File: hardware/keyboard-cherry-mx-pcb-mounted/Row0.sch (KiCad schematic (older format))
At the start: 28 parts, among them SW10 F4, SW11 F12, SW12 F5, SW13 Delete, SW14 F6, SW15 F7, SW2 ESC, SW3 F8, SW4 F1, SW5 F9, SW6 F2, SW7 F10, SW8 F3, SW9 F11

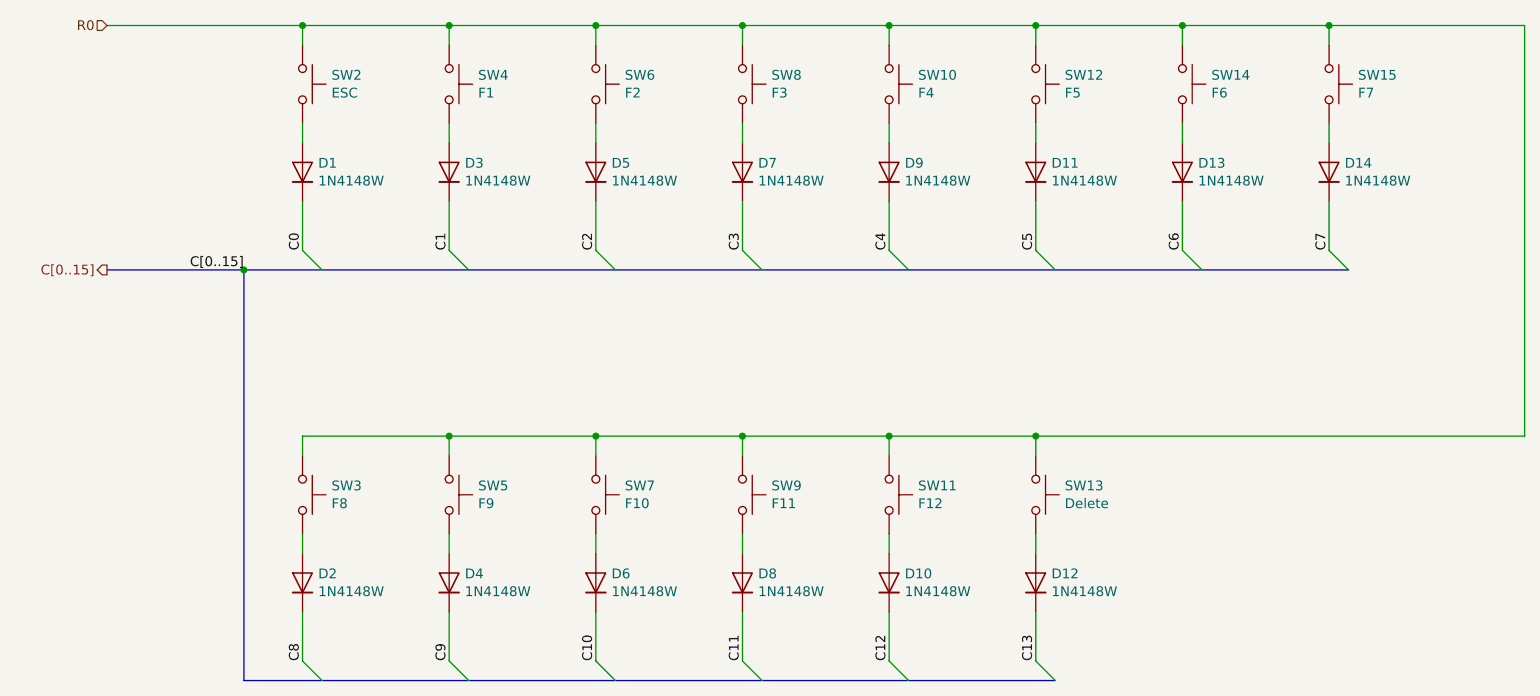
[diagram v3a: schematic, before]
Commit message: Aligns the keys so the column connections are more consistent. e.g. right most keys will have same column connection.
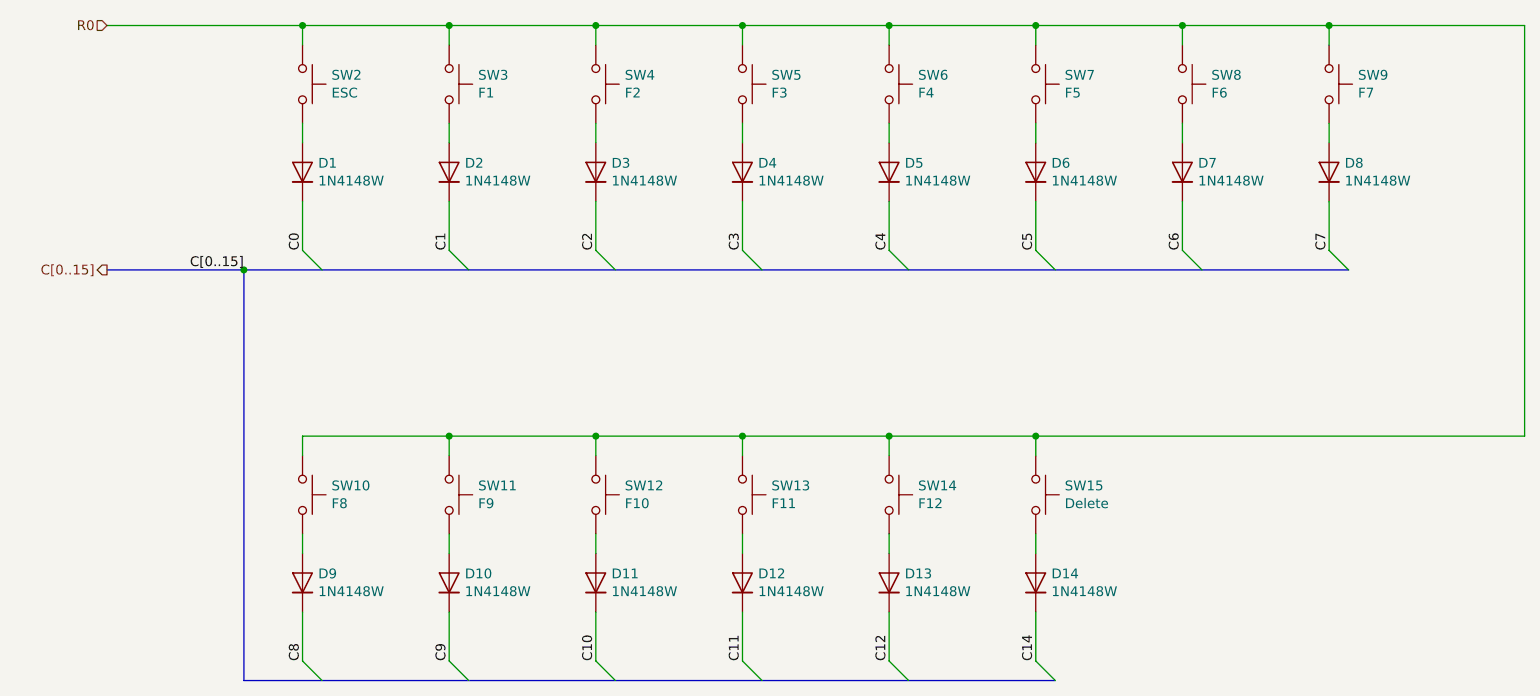
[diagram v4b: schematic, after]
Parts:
- renumbered D4 to D10, D6 to D11, D8 to D12, D10 to D13, D12 to D14, D3 to D2, D5 to D3, D7 to D4, D9 to D5, D11 to D6, D13 to D7, D14 to D8, D2 to D9, SW3 to SW10, SW5 to SW11, SW7 to SW12, SW9 to SW13, SW11 to SW14, SW13 to SW15, SW4 to SW3, SW6 to SW4, SW8 to SW5, SW10 to SW6, SW12 to SW7, SW14 to SW8, SW15 to SW9
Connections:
- net C13 renamed C14
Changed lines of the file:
@@
 P 3850 2700
 AR Path="/5E697948/5E6D9959" Ref="SW?"  Part="1"
-AR Path="/5E697948/5E6CDE4B/5E6D9959" Ref="SW4"  Part="1"
-F 0 "SW4" V 3804 2848 50  0000 L CNN
+AR Path="/5E697948/5E6CDE4B/5E6D9959" Ref="SW3"  Part="1"
+F 0 "SW3" V 3804 2848 50  0000 L CNN
 F 1 "F1" V 3895 2848 50  0000 L CNN
 F 2 "Button_Switch_Keyboard:SW_Cherry_MX_1.00u_PCB" H 3850 2900 50  0001 C CNN
@@
 P 3850 3150
 AR Path="/5E697948/5E6D995F" Ref="D?"  Part="1"
-AR Path="/5E697948/5E6CDE4B/5E6D995F" Ref="D3"  Part="1"
-F 0 "D3" V 3896 3070 50  0000 R CNN
+AR Path="/5E697948/5E6CDE4B/5E6D995F" Ref="D2"  Part="1"
+F 0 "D2" V 3896 3070 50  0000 R CNN
 F 1 "1N4148W" V 3805 3070 50  0000 R CNN
 F 2 "Diode_SMD:D_SOD-123" H 3850 2975 50  0001 C CNN
@@
 P 4600 2700
 AR Path="/5E697948/5E6D9967" Ref="SW?"  Part="1"
-AR Path="/5E697948/5E6CDE4B/5E6D9967" Ref="SW6"  Part="1"
-F 0 "SW6" V 4554 2848 50  0000 L CNN
+AR Path="/5E697948/5E6CDE4B/5E6D9967" Ref="SW4"  Part="1"
+F 0 "SW4" V 4554 2848 50  0000 L CNN
 F 1 "F2" V 4645 2848 50  0000 L CNN
 F 2 "Button_Switch_Keyboard:SW_Cherry_MX_1.00u_PCB" H 4600 2900 50  0001 C CNN
@@
 P 4600 3150
 AR Path="/5E697948/5E6D996D" Ref="D?"  Part="1"
-AR Path="/5E697948/5E6CDE4B/5E6D996D" Ref="D5"  Part="1"
-F 0 "D5" V 4646 3070 50  0000 R CNN
+AR Path="/5E697948/5E6CDE4B/5E6D996D" Ref="D3"  Part="1"
+F 0 "D3" V 4646 3070 50  0000 R CNN
 F 1 "1N4148W" V 4555 3070 50  0000 R CNN
 F 2 "Diode_SMD:D_SOD-123" H 4600 2975 50  0001 C CNN
@@
 P 5350 2700
 AR Path="/5E697948/5E6D9975" Ref="SW?"  Part="1"
-AR Path="/5E697948/5E6CDE4B/5E6D9975" Ref="SW8"  Part="1"
-F 0 "SW8" V 5304 2848 50  0000 L CNN
+AR Path="/5E697948/5E6CDE4B/5E6D9975" Ref="SW5"  Part="1"
+F 0 "SW5" V 5304 2848 50  0000 L CNN
 F 1 "F3" V 5395 2848 50  0000 L CNN
 F 2 "Button_Switch_Keyboard:SW_Cherry_MX_1.00u_PCB" H 5350 2900 50  0001 C CNN
@@
 P 5350 3150
 AR Path="/5E697948/5E6D997B" Ref="D?"  Part="1"
-AR Path="/5E697948/5E6CDE4B/5E6D997B" Ref="D7"  Part="1"
-F 0 "D7" V 5396 3070 50  0000 R CNN
+AR Path="/5E697948/5E6CDE4B/5E6D997B" Ref="D4"  Part="1"
+F 0 "D4" V 5396 3070 50  0000 R CNN
 F 1 "1N4148W" V 5305 3070 50  0000 R CNN
 F 2 "Diode_SMD:D_SOD-123" H 5350 2975 50  0001 C CNN
@@
 P 6100 2700
 AR Path="/5E697948/5E6D9983" Ref="SW?"  Part="1"
-AR Path="/5E697948/5E6CDE4B/5E6D9983" Ref="SW10"  Part="1"
-F 0 "SW10" V 6054 2848 50  0000 L CNN
+AR Path="/5E697948/5E6CDE4B/5E6D9983" Ref="SW6"  Part="1"
+F 0 "SW6" V 6054 2848 50  0000 L CNN
 F 1 "F4" V 6145 2848 50  0000 L CNN
 F 2 "Button_Switch_Keyboard:SW_Cherry_MX_1.00u_PCB" H 6100 2900 50  0001 C CNN
@@
 P 6100 3150
 AR Path="/5E697948/5E6D9989" Ref="D?"  Part="1"
-AR Path="/5E697948/5E6CDE4B/5E6D9989" Ref="D9"  Part="1"
-F 0 "D9" V 6146 3070 50  0000 R CNN
+AR Path="/5E697948/5E6CDE4B/5E6D9989" Ref="D5"  Part="1"
+F 0 "D5" V 6146 3070 50  0000 R CNN
 F 1 "1N4148W" V 6055 3070 50  0000 R CNN
 F 2 "Diode_SMD:D_SOD-123" H 6100 2975 50  0001 C CNN
@@
 P 6850 2700
 AR Path="/5E697948/5E6D9991" Ref="SW?"  Part="1"
-AR Path="/5E697948/5E6CDE4B/5E6D9991" Ref="SW12"  Part="1"
-F 0 "SW12" V 6804 2848 50  0000 L CNN
+AR Path="/5E697948/5E6CDE4B/5E6D9991" Ref="SW7"  Part="1"
+F 0 "SW7" V 6804 2848 50  0000 L CNN
 F 1 "F5" V 6895 2848 50  0000 L CNN
 F 2 "Button_Switch_Keyboard:SW_Cherry_MX_1.00u_PCB" H 6850 2900 50  0001 C CNN
@@
 P 6850 3150
 AR Path="/5E697948/5E6D9997" Ref="D?"  Part="1"
-AR Path="/5E697948/5E6CDE4B/5E6D9997" Ref="D11"  Part="1"
-F 0 "D11" V 6896 3070 50  0000 R CNN
+AR Path="/5E697948/5E6CDE4B/5E6D9997" Ref="D6"  Part="1"
+F 0 "D6" V 6896 3070 50  0000 R CNN
 F 1 "1N4148W" V 6805 3070 50  0000 R CNN
 F 2 "Diode_SMD:D_SOD-123" H 6850 2975 50  0001 C CNN
@@
 P 7600 2700
 AR Path="/5E697948/5E6D999F" Ref="SW?"  Part="1"
-AR Path="/5E697948/5E6CDE4B/5E6D999F" Ref="SW14"  Part="1"
-F 0 "SW14" V 7554 2848 50  0000 L CNN
+AR Path="/5E697948/5E6CDE4B/5E6D999F" Ref="SW8"  Part="1"
+F 0 "SW8" V 7554 2848 50  0000 L CNN
 F 1 "F6" V 7645 2848 50  0000 L CNN
 F 2 "Button_Switch_Keyboard:SW_Cherry_MX_1.00u_PCB" H 7600 2900 50  0001 C CNN
@@
 P 7600 3150
 AR Path="/5E697948/5E6D99A5" Ref="D?"  Part="1"
-AR Path="/5E697948/5E6CDE4B/5E6D99A5" Ref="D13"  Part="1"
-F 0 "D13" V 7646 3070 50  0000 R CNN
+AR Path="/5E697948/5E6CDE4B/5E6D99A5" Ref="D7"  Part="1"
+F 0 "D7" V 7646 3070 50  0000 R CNN
 F 1 "1N4148W" V 7555 3070 50  0000 R CNN
 F 2 "Diode_SMD:D_SOD-123" H 7600 2975 50  0001 C CNN
@@
 P 8350 2700
 AR Path="/5E697948/5E6D99AD" Ref="SW?"  Part="1"
-AR Path="/5E697948/5E6CDE4B/5E6D99AD" Ref="SW15"  Part="1"
-F 0 "SW15" V 8304 2848 50  0000 L CNN
+AR Path="/5E697948/5E6CDE4B/5E6D99AD" Ref="SW9"  Part="1"
+F 0 "SW9" V 8304 2848 50  0000 L CNN
 F 1 "F7" V 8395 2848 50  0000 L CNN
 F 2 "Button_Switch_Keyboard:SW_Cherry_MX_1.00u_PCB" H 8350 2900 50  0001 C CNN
@@
 P 8350 3150
 AR Path="/5E697948/5E6D99B3" Ref="D?"  Part="1"
-AR Path="/5E697948/5E6CDE4B/5E6D99B3" Ref="D14"  Part="1"
-F 0 "D14" V 8396 3070 50  0000 R CNN
+AR Path="/5E697948/5E6CDE4B/5E6D99B3" Ref="D8"  Part="1"
+F 0 "D8" V 8396 3070 50  0000 R CNN
 F 1 "1N4148W" V 8305 3070 50  0000 R CNN
 F 2 "Diode_SMD:D_SOD-123" H 8350 2975 50  0001 C CNN
@@
 P 3100 4800
 AR Path="/5E697948/5E6D99BB" Ref="SW?"  Part="1"
-AR Path="/5E697948/5E6CDE4B/5E6D99BB" Ref="SW3"  Part="1"
-F 0 "SW3" V 3054 4948 50  0000 L CNN
+AR Path="/5E697948/5E6CDE4B/5E6D99BB" Ref="SW10"  Part="1"
+F 0 "SW10" V 3054 4948 50  0000 L CNN
 F 1 "F8" V 3145 4948 50  0000 L CNN
 F 2 "Button_Switch_Keyboard:SW_Cherry_MX_1.00u_PCB" H 3100 5000 50  0001 C CNN
@@
 P 3100 5250
 AR Path="/5E697948/5E6D99C1" Ref="D?"  Part="1"
-AR Path="/5E697948/5E6CDE4B/5E6D99C1" Ref="D2"  Part="1"
-F 0 "D2" V 3146 5170 50  0000 R CNN
+AR Path="/5E697948/5E6CDE4B/5E6D99C1" Ref="D9"  Part="1"
+F 0 "D9" V 3146 5170 50  0000 R CNN
 F 1 "1N4148W" V 3055 5170 50  0000 R CNN
 F 2 "Diode_SMD:D_SOD-123" H 3100 5075 50  0001 C CNN
@@
 P 3850 4800
 AR Path="/5E697948/5E6D99C9" Ref="SW?"  Part="1"
-AR Path="/5E697948/5E6CDE4B/5E6D99C9" Ref="SW5"  Part="1"
-F 0 "SW5" V 3804 4948 50  0000 L CNN
+AR Path="/5E697948/5E6CDE4B/5E6D99C9" Ref="SW11"  Part="1"
+F 0 "SW11" V 3804 4948 50  0000 L CNN
 F 1 "F9" V 3895 4948 50  0000 L CNN
 F 2 "Button_Switch_Keyboard:SW_Cherry_MX_1.00u_PCB" H 3850 5000 50  0001 C CNN
@@
 P 3850 5250
 AR Path="/5E697948/5E6D99CF" Ref="D?"  Part="1"
-AR Path="/5E697948/5E6CDE4B/5E6D99CF" Ref="D4"  Part="1"
-F 0 "D4" V 3896 5170 50  0000 R CNN
+AR Path="/5E697948/5E6CDE4B/5E6D99CF" Ref="D10"  Part="1"
+F 0 "D10" V 3896 5170 50  0000 R CNN
 F 1 "1N4148W" V 3805 5170 50  0000 R CNN
 F 2 "Diode_SMD:D_SOD-123" H 3850 5075 50  0001 C CNN
@@
 P 4600 4800
 AR Path="/5E697948/5E6D99D7" Ref="SW?"  Part="1"
-AR Path="/5E697948/5E6CDE4B/5E6D99D7" Ref="SW7"  Part="1"
-F 0 "SW7" V 4554 4948 50  0000 L CNN
+AR Path="/5E697948/5E6CDE4B/5E6D99D7" Ref="SW12"  Part="1"
+F 0 "SW12" V 4554 4948 50  0000 L CNN
 F 1 "F10" V 4645 4948 50  0000 L CNN
 F 2 "Button_Switch_Keyboard:SW_Cherry_MX_1.00u_PCB" H 4600 5000 50  0001 C CNN
@@
 P 4600 5250
 AR Path="/5E697948/5E6D99DD" Ref="D?"  Part="1"
-AR Path="/5E697948/5E6CDE4B/5E6D99DD" Ref="D6"  Part="1"
-F 0 "D6" V 4646 5170 50  0000 R CNN
+AR Path="/5E697948/5E6CDE4B/5E6D99DD" Ref="D11"  Part="1"
+F 0 "D11" V 4646 5170 50  0000 R CNN
 F 1 "1N4148W" V 4555 5170 50  0000 R CNN
 F 2 "Diode_SMD:D_SOD-123" H 4600 5075 50  0001 C CNN
@@
 P 5350 4800
 AR Path="/5E697948/5E6D99E5" Ref="SW?"  Part="1"
-AR Path="/5E697948/5E6CDE4B/5E6D99E5" Ref="SW9"  Part="1"
-F 0 "SW9" V 5304 4948 50  0000 L CNN
+AR Path="/5E697948/5E6CDE4B/5E6D99E5" Ref="SW13"  Part="1"
+F 0 "SW13" V 5304 4948 50  0000 L CNN
 F 1 "F11" V 5395 4948 50  0000 L CNN
 F 2 "Button_Switch_Keyboard:SW_Cherry_MX_1.00u_PCB" H 5350 5000 50  0001 C CNN
@@
 P 5350 5250
 AR Path="/5E697948/5E6D99EB" Ref="D?"  Part="1"
-AR Path="/5E697948/5E6CDE4B/5E6D99EB" Ref="D8"  Part="1"
-F 0 "D8" V 5396 5170 50  0000 R CNN
+AR Path="/5E697948/5E6CDE4B/5E6D99EB" Ref="D12"  Part="1"
+F 0 "D12" V 5396 5170 50  0000 R CNN
 F 1 "1N4148W" V 5305 5170 50  0000 R CNN
 F 2 "Diode_SMD:D_SOD-123" H 5350 5075 50  0001 C CNN
@@
 P 6100 4800
 AR Path="/5E697948/5E6D99F3" Ref="SW?"  Part="1"
-AR Path="/5E697948/5E6CDE4B/5E6D99F3" Ref="SW11"  Part="1"
-F 0 "SW11" V 6054 4948 50  0000 L CNN
+AR Path="/5E697948/5E6CDE4B/5E6D99F3" Ref="SW14"  Part="1"
+F 0 "SW14" V 6054 4948 50  0000 L CNN
 F 1 "F12" V 6145 4948 50  0000 L CNN
 F 2 "Button_Switch_Keyboard:SW_Cherry_MX_1.00u_PCB" H 6100 5000 50  0001 C CNN
@@
 P 6100 5250
 AR Path="/5E697948/5E6D99F9" Ref="D?"  Part="1"
-AR Path="/5E697948/5E6CDE4B/5E6D99F9" Ref="D10"  Part="1"
-F 0 "D10" V 6146 5170 50  0000 R CNN
+AR Path="/5E697948/5E6CDE4B/5E6D99F9" Ref="D13"  Part="1"
+F 0 "D13" V 6146 5170 50  0000 R CNN
 F 1 "1N4148W" V 6055 5170 50  0000 R CNN
 F 2 "Diode_SMD:D_SOD-123" H 6100 5075 50  0001 C CNN
@@
 P 6850 4800
 AR Path="/5E697948/5E6D9A01" Ref="SW?"  Part="1"
-AR Path="/5E697948/5E6CDE4B/5E6D9A01" Ref="SW13"  Part="1"
-F 0 "SW13" V 6804 4948 50  0000 L CNN
+AR Path="/5E697948/5E6CDE4B/5E6D9A01" Ref="SW15"  Part="1"
+F 0 "SW15" V 6804 4948 50  0000 L CNN
 F 1 "Delete" V 6895 4948 50  0000 L CNN
 F 2 "Button_Switch_Keyboard:SW_Cherry_MX_1.00u_PCB" H 6850 5000 50  0001 C CNN
@@
 P 6850 5250
 AR Path="/5E697948/5E6D9A07" Ref="D?"  Part="1"
-AR Path="/5E697948/5E6CDE4B/5E6D9A07" Ref="D12"  Part="1"
-F 0 "D12" V 6896 5170 50  0000 R CNN
+AR Path="/5E697948/5E6CDE4B/5E6D9A07" Ref="D14"  Part="1"
+F 0 "D14" V 6896 5170 50  0000 R CNN
 F 1 "1N4148W" V 6805 5170 50  0000 R CNN
 F 2 "Diode_SMD:D_SOD-123" H 6850 5075 50  0001 C CNN
@@
 C12
 Text Label 6850 5650 1    50   ~ 0
-C13
+C14
 Entry Wire Line
 	3100 3550 3200 3650

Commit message: Adds labels for each key and creates gerber files.
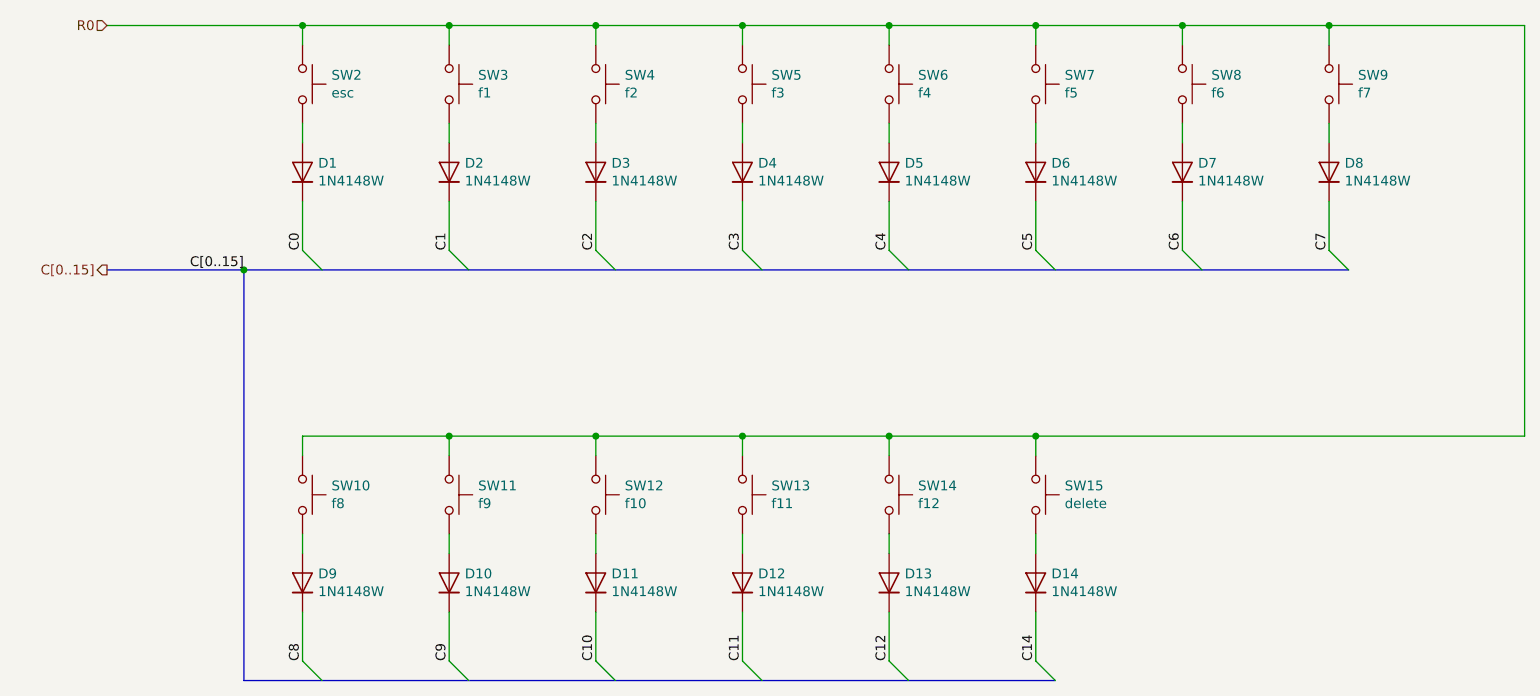
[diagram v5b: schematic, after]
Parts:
- SW10: value F8 -> f8
- SW11: value F9 -> f9
- SW12: value F10 -> f10
- SW13: value F11 -> f11
- SW14: value F12 -> f12
- SW15: value Delete -> delete
- SW2: value ESC -> esc
- SW3: value F1 -> f1
- SW4: value F2 -> f2
- SW5: value F3 -> f3
- SW6: value F4 -> f4
- SW7: value F5 -> f5
- SW8: value F6 -> f6
- SW9: value F7 -> f7
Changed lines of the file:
@@
 AR Path="/5E697948/5E6CDE4B/5E6D9949" Ref="SW2"  Part="1"
 F 0 "SW2" V 3054 2848 50  0000 L CNN
-F 1 "ESC" V 3145 2848 50  0000 L CNN
+F 1 "esc" V 3145 2848 50  0000 L CNN
 F 2 "Button_Switch_Keyboard:SW_Cherry_MX_1.00u_PCB" H 3100 2900 50  0001 C CNN
 F 3 "~" H 3100 2900 50  0001 C CNN
@@
 AR Path="/5E697948/5E6CDE4B/5E6D9959" Ref="SW3"  Part="1"
 F 0 "SW3" V 3804 2848 50  0000 L CNN
-F 1 "F1" V 3895 2848 50  0000 L CNN
+F 1 "f1" V 3895 2848 50  0000 L CNN
 F 2 "Button_Switch_Keyboard:SW_Cherry_MX_1.00u_PCB" H 3850 2900 50  0001 C CNN
 F 3 "~" H 3850 2900 50  0001 C CNN
@@
 AR Path="/5E697948/5E6CDE4B/5E6D9967" Ref="SW4"  Part="1"
 F 0 "SW4" V 4554 2848 50  0000 L CNN
-F 1 "F2" V 4645 2848 50  0000 L CNN
+F 1 "f2" V 4645 2848 50  0000 L CNN
 F 2 "Button_Switch_Keyboard:SW_Cherry_MX_1.00u_PCB" H 4600 2900 50  0001 C CNN
 F 3 "~" H 4600 2900 50  0001 C CNN
@@
 AR Path="/5E697948/5E6CDE4B/5E6D9975" Ref="SW5"  Part="1"
 F 0 "SW5" V 5304 2848 50  0000 L CNN
-F 1 "F3" V 5395 2848 50  0000 L CNN
+F 1 "f3" V 5395 2848 50  0000 L CNN
 F 2 "Button_Switch_Keyboard:SW_Cherry_MX_1.00u_PCB" H 5350 2900 50  0001 C CNN
 F 3 "~" H 5350 2900 50  0001 C CNN
@@
 AR Path="/5E697948/5E6CDE4B/5E6D9983" Ref="SW6"  Part="1"
 F 0 "SW6" V 6054 2848 50  0000 L CNN
-F 1 "F4" V 6145 2848 50  0000 L CNN
+F 1 "f4" V 6145 2848 50  0000 L CNN
 F 2 "Button_Switch_Keyboard:SW_Cherry_MX_1.00u_PCB" H 6100 2900 50  0001 C CNN
 F 3 "~" H 6100 2900 50  0001 C CNN
@@
 AR Path="/5E697948/5E6CDE4B/5E6D9991" Ref="SW7"  Part="1"
 F 0 "SW7" V 6804 2848 50  0000 L CNN
-F 1 "F5" V 6895 2848 50  0000 L CNN
+F 1 "f5" V 6895 2848 50  0000 L CNN
 F 2 "Button_Switch_Keyboard:SW_Cherry_MX_1.00u_PCB" H 6850 2900 50  0001 C CNN
 F 3 "~" H 6850 2900 50  0001 C CNN
@@
 AR Path="/5E697948/5E6CDE4B/5E6D999F" Ref="SW8"  Part="1"
 F 0 "SW8" V 7554 2848 50  0000 L CNN
-F 1 "F6" V 7645 2848 50  0000 L CNN
+F 1 "f6" V 7645 2848 50  0000 L CNN
 F 2 "Button_Switch_Keyboard:SW_Cherry_MX_1.00u_PCB" H 7600 2900 50  0001 C CNN
 F 3 "~" H 7600 2900 50  0001 C CNN
@@
 AR Path="/5E697948/5E6CDE4B/5E6D99AD" Ref="SW9"  Part="1"
 F 0 "SW9" V 8304 2848 50  0000 L CNN
-F 1 "F7" V 8395 2848 50  0000 L CNN
+F 1 "f7" V 8395 2848 50  0000 L CNN
 F 2 "Button_Switch_Keyboard:SW_Cherry_MX_1.00u_PCB" H 8350 2900 50  0001 C CNN
 F 3 "~" H 8350 2900 50  0001 C CNN
@@
 AR Path="/5E697948/5E6CDE4B/5E6D99BB" Ref="SW10"  Part="1"
 F 0 "SW10" V 3054 4948 50  0000 L CNN
-F 1 "F8" V 3145 4948 50  0000 L CNN
+F 1 "f8" V 3145 4948 50  0000 L CNN
 F 2 "Button_Switch_Keyboard:SW_Cherry_MX_1.00u_PCB" H 3100 5000 50  0001 C CNN
 F 3 "~" H 3100 5000 50  0001 C CNN
@@
 AR Path="/5E697948/5E6CDE4B/5E6D99C9" Ref="SW11"  Part="1"
 F 0 "SW11" V 3804 4948 50  0000 L CNN
-F 1 "F9" V 3895 4948 50  0000 L CNN
+F 1 "f9" V 3895 4948 50  0000 L CNN
 F 2 "Button_Switch_Keyboard:SW_Cherry_MX_1.00u_PCB" H 3850 5000 50  0001 C CNN
 F 3 "~" H 3850 5000 50  0001 C CNN
@@
 AR Path="/5E697948/5E6CDE4B/5E6D99D7" Ref="SW12"  Part="1"
 F 0 "SW12" V 4554 4948 50  0000 L CNN
-F 1 "F10" V 4645 4948 50  0000 L CNN
+F 1 "f10" V 4645 4948 50  0000 L CNN
 F 2 "Button_Switch_Keyboard:SW_Cherry_MX_1.00u_PCB" H 4600 5000 50  0001 C CNN
 F 3 "~" H 4600 5000 50  0001 C CNN
@@
 AR Path="/5E697948/5E6CDE4B/5E6D99E5" Ref="SW13"  Part="1"
 F 0 "SW13" V 5304 4948 50  0000 L CNN
-F 1 "F11" V 5395 4948 50  0000 L CNN
+F 1 "f11" V 5395 4948 50  0000 L CNN
 F 2 "Button_Switch_Keyboard:SW_Cherry_MX_1.00u_PCB" H 5350 5000 50  0001 C CNN
 F 3 "~" H 5350 5000 50  0001 C CNN
@@
 AR Path="/5E697948/5E6CDE4B/5E6D99F3" Ref="SW14"  Part="1"
 F 0 "SW14" V 6054 4948 50  0000 L CNN
-F 1 "F12" V 6145 4948 50  0000 L CNN
+F 1 "f12" V 6145 4948 50  0000 L CNN
 F 2 "Button_Switch_Keyboard:SW_Cherry_MX_1.00u_PCB" H 6100 5000 50  0001 C CNN
 F 3 "~" H 6100 5000 50  0001 C CNN
@@
 AR Path="/5E697948/5E6CDE4B/5E6D9A01" Ref="SW15"  Part="1"
 F 0 "SW15" V 6804 4948 50  0000 L CNN
-F 1 "Delete" V 6895 4948 50  0000 L CNN
+F 1 "delete" V 6895 4948 50  0000 L CNN
 F 2 "Button_Switch_Keyboard:SW_Cherry_MX_1.00u_PCB" H 6850 5000 50  0001 C CNN
 F 3 "~" H 6850 5000 50  0001 C CNN
